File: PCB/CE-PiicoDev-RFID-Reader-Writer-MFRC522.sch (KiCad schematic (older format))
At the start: 63 parts, among them J1 , J2 , J3 Conn_PiicoDev_header_01x04_Ma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, J4 Conn_01x01_Male, J5 Conn_01x01_Male, Q1 BSS138, U1 MFRC522, Y1 27.12MHz 12pF

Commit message: Improve Artwork
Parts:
- added G6: Label_PCB_Art, PiicoDev RFID MFRC522:Art_1, symbol CoreElectronics_Artwork:Label_PCB_Art
- added G7: Label_PCB_Art, PiicoDev RFID MFRC522:Art_2, symbol CoreElectronics_Artwork:Label_PCB_Art
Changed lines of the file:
@@
 Wire Wire Line
 	5400 3500 5400 3400
+$Comp
+L CoreElectronics_Artwork:Label_PCB_Art G7
+U 1 1 61AF4072
+P 4150 6650
+F 0 "G7" H 4278 6696 50  0000 L CNN
+F 1 "Label_PCB_Art" H 4278 6605 50  0000 L CNN
+F 2 "PiicoDev RFID MFRC522:Art_2" H 4150 6650 50  0001 C CNN
+F 3 "" H 4150 6650 50  0001 C CNN
+	1    4150 6650
+	1    0    0    -1
+$EndComp
+$Comp
+L CoreElectronics_Artwork:Label_PCB_Art G6
+U 1 1 61AF4D20
+P 4150 6400
+F 0 "G6" H 4278 6446 50  0000 L CNN
+F 1 "Label_PCB_Art" H 4278 6355 50  0000 L CNN
+F 2 "PiicoDev RFID MFRC522:Art_1" H 4150 6400 50  0001 C CNN
+F 3 "" H 4150 6400 50  0001 C CNN
+	1    4150 6400
+	1    0    0    -1
+$EndComp
 $EndSCHEMATC

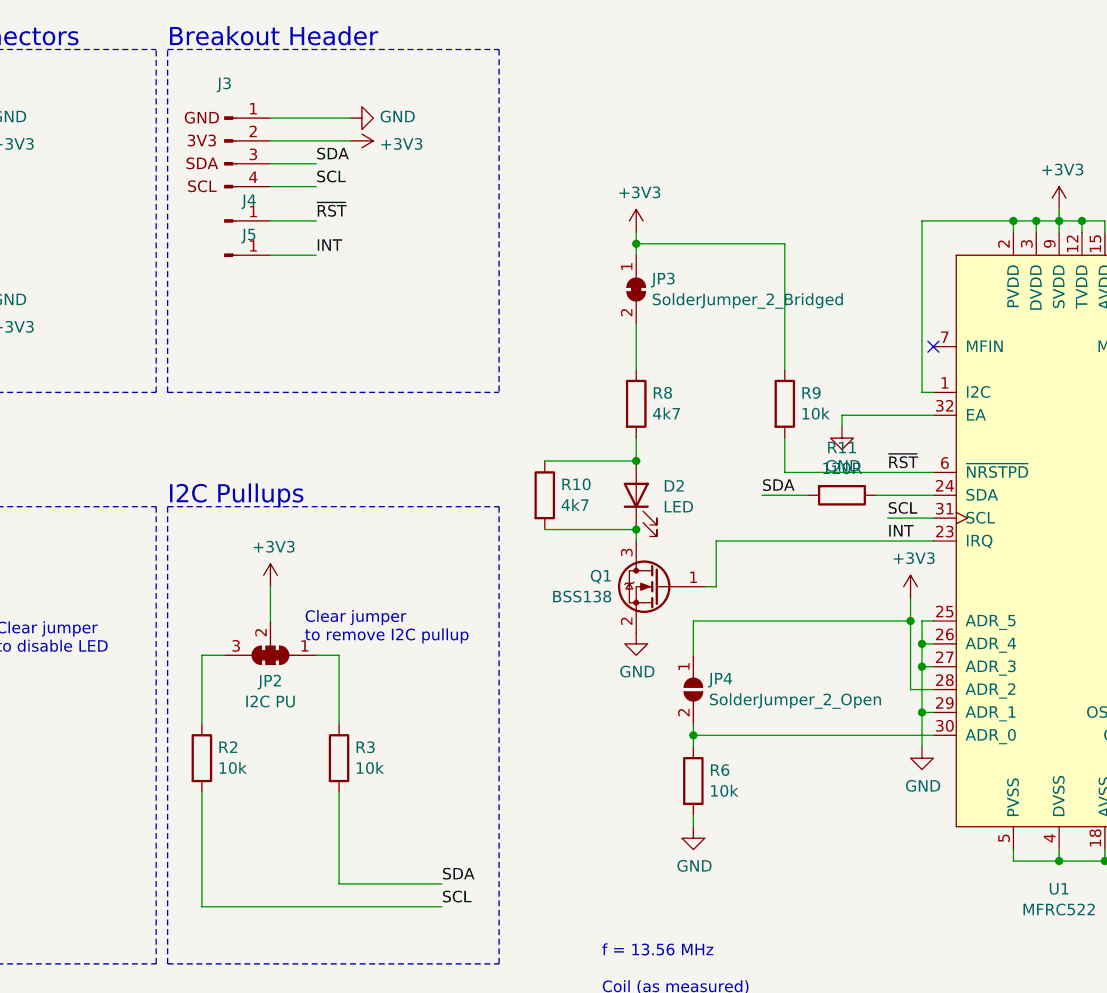
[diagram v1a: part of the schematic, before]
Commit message: Remove Interrupt LED and add DIP switches
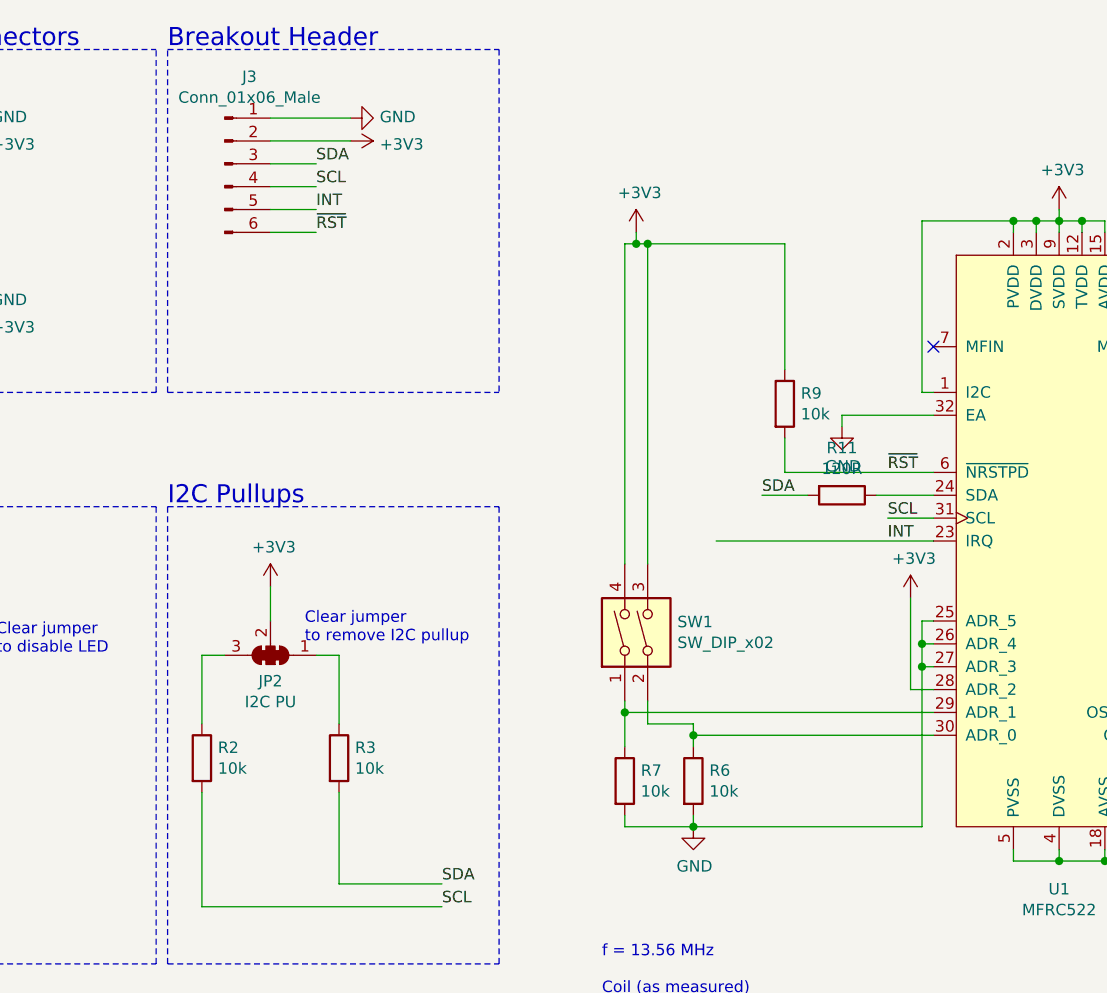
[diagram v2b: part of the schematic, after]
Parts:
- removed D2: LED, CoreElectronics_Components:LED_1206_3216Metric_ReverseMount_Hole1.8x2.4mm, symbol Device:LED
- removed J3: Conn_PiicoDev_header_01x04_Male, CoreElectronics_Components:PiicoDev_header_4pin, symbol CoreElectronics_Components:Conn_PiicoDev_header_01x04_Male
- removed J4: Conn_01x01_Male, CoreElectronics_Components:PiicoDev_header_1pin, symbol Connector:Conn_01x01_Male
- removed J5: Conn_01x01_Male, CoreElectronics_Components:PiicoDev_header_1pin_INT_uninverted, symbol Connector:Conn_01x01_Male
- removed JP3: SolderJumper_2_Bridged, CoreElectronics_Components:SolderJumper-2_P1.3mm_Bridged_RoundedPad1.0x1.5mm, symbol Jumper:SolderJumper_2_Bridged
- removed JP4: SolderJumper_2_Open, CoreElectronics_Components:SolderJumper-2_P1.3mm_Open_RoundedPad1.0x1.5mm, symbol Jumper:SolderJumper_2_Open
- removed Q1: BSS138, Package_TO_SOT_SMD:SOT-23, symbol Transistor_FET:BSS138
- removed R10, R8: 4k7, Resistor_SMD:R_0402_1005Metric, symbol Device:R
- added J3: Conn_01x06_Male, CoreElectronics_Components:PiicoDev_header_6pin, symbol Connector:Conn_01x06_Male
- added R7: 10k, Resistor_SMD:R_0402_1005Metric, symbol Device:R
- added SW1: SW_DIP_x02, CoreElectronics_Components:SW_DIP_x02_Slide_CHS-02A1, symbol Switch:SW_DIP_x02
- G2: footprint CoreElectronics_Artwork:CoreElectronics_logo_5mm -> (none)
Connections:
- net +3V3: now also J3.2 (Pin_2), SW1.3, SW1.4
- net GND: now also J3.1 (Pin_1), R7.2; no longer U1.29 (ADR_1)
- net INT: now also J3.5 (Pin_5)
- net SCL: now also J3.4 (Pin_4)
- net SDA: now also J3.3 (Pin_3)
- net ~RST: now also J3.6 (Pin_6)
- net at R6.1, U1.30 (ADR_0): now also SW1.2
- new net: R7.1, SW1.1, U1.29 (ADR_1)
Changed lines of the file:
@@
 Sheet 1 1
 Title "PiicoDev RFID Reader/Writer MFRC522"
-Date "2021-11-26"
-Rev "02"
+Date "2021-12-14"
+Rev "03"
 Comp "Core Electronics"
 Comment1 "Designed at Core Electronics by Peter Johnston"
@@
 F 0 "G2" H 9900 6044 60  0001 C CNN
 F 1 "LOGO_CoreElectronics_no-text" H 9900 6456 60  0001 C CNN
-F 2 "CoreElectronics_Artwork:CoreElectronics_logo_5mm" H 9900 6250 50  0001 C CNN
+F 2 "" H 9900 6250 50  0001 C CNN
 F 3 "" H 9900 6250 50  0001 C CNN
 	1    9900 6250
@@
 Text Label 2800 1600 0    50   ~ 0
 SCL
-Wire Wire Line
-	2800 1600 2600 1600
 Text Label 2800 1500 0    50   ~ 0
 SDA
-Wire Wire Line
-	2800 1500 2600 1500
 $Comp
 L power:+3V3 #PWR?
@@
 	0    -1   -1   0
 $EndComp
-Wire Wire Line
-	2950 1300 2600 1300
-Wire Wire Line
-	2600 1400 2950 1400
 Text Notes 650  1000 0    79   ~ 0
 PiicoDev Connectors
 Text Notes 2150 1000 0    79   ~ 0
 Breakout Header
-$Comp
-L CoreElectronics_Components:Conn_PiicoDev_header_01x04_Male J?
-U 1 1 609F9B2E
-P 2400 1500
-AR Path="/609C5735/609F9B2E" Ref="J?"  Part="1"
-AR Path="/609F9B2E" Ref="J3"  Part="1"
-F 0 "J3" H 2400 1850 50  0000 C CNN
-F 1 "Conn_PiicoDev_header_01x04_Male" H 2421 1807 50  0001 C CNN
-F 2 "CoreElectronics_Components:PiicoDev_header_4pin" H 2400 1500 50  0001 C CNN
-F 3 "~" H 2400 1500 50  0001 C CNN
-	1    2400 1500
-	1    0    0    -1
-$EndComp
 Wire Notes Line
 	650  2500 650  1000
@@
 	1    0    0    -1
 $EndComp
-$Comp
-L Connector:Conn_01x01_Male J4
-U 1 1 6159070E
-P 2400 1750
-F 0 "J4" H 2508 1839 50  0000 C CNN
-F 1 "Conn_01x01_Male" H 2508 1840 50  0001 C CNN
-F 2 "CoreElectronics_Components:PiicoDev_header_1pin" H 2400 1750 50  0001 C CNN
-F 3 "~" H 2400 1750 50  0001 C CNN
-	1    2400 1750
-	1    0    0    -1
-$EndComp
-$Comp
-L Connector:Conn_01x01_Male J5
-U 1 1 61591567
-P 2400 1900
-F 0 "J5" H 2508 1989 50  0000 C CNN
-F 1 "Conn_01x01_Male" H 2508 1990 50  0001 C CNN
-F 2 "CoreElectronics_Components:PiicoDev_header_1pin_INT_uninverted" H 2400 1900 50  0001 C CNN
-F 3 "~" H 2400 1900 50  0001 C CNN
-	1    2400 1900
-	1    0    0    -1
-$EndComp
-Wire Wire Line
-	2600 1750 2800 1750
-Wire Wire Line
-	2600 1900 2800 1900
-Text Label 2800 1750 0    50   ~ 0
+Text Label 2800 1800 0    50   ~ 0
 ~RST
-Text Label 2800 1900 0    50   ~ 0
+Text Label 2800 1700 0    50   ~ 0
 INT
 Wire Wire Line
 	8150 4550 8150 4600
 Connection ~ 8150 4550
-$Comp
-L Device:LED D2
-U 1 1 6138F2E9
-P 4200 2950
-F 0 "D2" V 4239 2832 50  0000 R CNN
-F 1 "LED" V 4148 2832 50  0000 R CNN
-F 2 "CoreElectronics_Components:LED_1206_3216Metric_ReverseMount_Hole1.8x2.4mm" H 4200 2950 50  0001 C CNN
-F 3 "~" H 4200 2950 50  0001 C CNN
-	1    4200 2950
-	0    -1   -1   0
-$EndComp
-$Comp
-L Device:R R8
-U 1 1 61390113
-P 4200 2550
-F 0 "R8" H 4270 2596 50  0000 L CNN
-F 1 "4k7" H 4270 2505 50  0000 L CNN
-F 2 "Resistor_SMD:R_0402_1005Metric" V 4130 2550 50  0001 C CNN
-F 3 "~" H 4200 2550 50  0001 C CNN
-	1    4200 2550
-	1    0    0    -1
-$EndComp
 $Comp
 L power:+3V3 #PWR0113
@@
 $EndComp
 Wire Wire Line
-	4200 2700 4200 2800
-$Comp
-L Jumper:SolderJumper_2_Bridged JP3
-U 1 1 613A247F
-P 4200 2050
-F 0 "JP3" V 4154 2118 50  0000 L CNN
-F 1 "SolderJumper_2_Bridged" V 4245 2118 50  0000 L CNN
-F 2 "CoreElectronics_Components:SolderJumper-2_P1.3mm_Bridged_RoundedPad1.0x1.5mm" H 4200 2050 50  0001 C CNN
-F 3 "~" H 4200 2050 50  0001 C CNN
-	1    4200 2050
-	0    1    1    0
-$EndComp
-Wire Wire Line
 	4200 1800 4200 1850
-Wire Wire Line
-	4200 2200 4200 2400
-Wire Wire Line
-	4200 3150 4200 3100
 $Comp
 L power:GND #PWR0114
@@
 $EndComp
 Wire Wire Line
-	4200 1850 4850 1850
+	4200 1850 4250 1850
 Wire Wire Line
 	4850 1850 4850 2400
-Connection ~ 4200 1850
-Wire Wire Line
-	4200 1850 4200 1900
 Wire Wire Line
 	4850 2700 4850 2850
@@
 Text Label 10400 3150 0    50   ~ 0
 TURN6A
-Wire Wire Line
-	4550 3150 4550 3350
-Wire Wire Line
-	4550 3350 4500 3350
-$Comp
-L power:GND #PWR05
-U 1 1 6175382D
-P 4200 3550
-F 0 "#PWR05" H 4200 3300 50  0001 C CNN
-F 1 "GND" H 4205 3377 50  0000 C CNN
-F 2 "" H 4200 3550 50  0001 C CNN
-F 3 "" H 4200 3550 50  0001 C CNN
-	1    4200 3550
-	1    0    0    -1
-$EndComp
-$Comp
-L Device:R R10
-U 1 1 6175452D
-P 3800 2950
-F 0 "R10" H 3870 2996 50  0000 L CNN
-F 1 "4k7" H 3870 2905 50  0000 L CNN
-F 2 "Resistor_SMD:R_0402_1005Metric" V 3730 2950 50  0001 C CNN
-F 3 "~" H 3800 2950 50  0001 C CNN
-	1    3800 2950
-	1    0    0    -1
-$EndComp
-Wire Wire Line
-	3800 2800 4200 2800
-Connection ~ 4200 2800
-Wire Wire Line
-	3800 3100 4200 3100
-Connection ~ 4200 3100
 $Comp
 L CoreElectronics_Artwork:Label_PCB_Art G4
@@
 /Design Files/MFRC522.m
 Wire Wire Line
-	4550 3150 5500 3150
-Wire Wire Line
 	4850 2850 5500 2850
-$Comp
-L Transistor_FET:BSS138 Q1
-U 1 1 61721C80
-P 4300 3350
-F 0 "Q1" H 4505 3396 50  0000 L CNN
-F 1 "BSS138" H 4505 3305 50  0000 L CNN
-F 2 "Package_TO_SOT_SMD:SOT-23" H 4500 3275 50  0001 L CIN
-F 3 "https://www.onsemi.com/pub/Collateral/BSS138-D.PDF" H 4300 3350 50  0001 L CNN
-	1    4300 3350
-	-1   0    0    -1
-$EndComp
 $Comp
 L Device:Net-Tie_2 NT8
@@
 Wire Wire Line
 	5500 3700 5450 3700
-Connection ~ 5450 3700
-Wire Wire Line
-	5500 3900 5450 3900
-Connection ~ 5450 3900
-$Comp
-L power:GND #PWR0116
-U 1 1 61A25A71
-P 5450 4050
-F 0 "#PWR0116" H 5450 3800 50  0001 C CNN
-F 1 "GND" H 5455 3877 50  0000 C CNN
-F 2 "" H 5450 4050 50  0001 C CNN
-F 3 "" H 5450 4050 50  0001 C CNN
-	1    5450 4050
-	1    0    0    -1
-$EndComp
 Wire Wire Line
 	8100 2750 8700 2750
@@
 	9450 3550 10400 3550
 Wire Wire Line
-	5450 3700 5450 3900
-Wire Wire Line
 	5500 3800 5400 3800
-Wire Wire Line
-	5400 3800 5400 3500
 $Comp
 L power:+3V3 #PWR0117
@@
 $EndComp
 $Comp
-L Jumper:SolderJumper_2_Open JP4
-U 1 1 61A874F4
-P 4450 3800
-F 0 "JP4" V 4404 3868 50  0000 L CNN
-F 1 "SolderJumper_2_Open" V 4495 3868 50  0000 L CNN
-F 2 "CoreElectronics_Components:SolderJumper-2_P1.3mm_Open_RoundedPad1.0x1.5mm" H 4450 3800 50  0001 C CNN
-F 3 "~" H 4450 3800 50  0001 C CNN
-	1    4450 3800
-	0    1    1    0
-$EndComp
-Wire Wire Line
-	5450 3900 5450 4050
-$Comp
 L Device:R R6
 U 1 1 61A91638
@@
 Wire Wire Line
 	4450 4350 4450 4400
-Wire Wire Line
-	4450 4000 4450 3950
 Connection ~ 4450 4000
-Wire Wire Line
-	4450 3650 4450 3500
-Wire Wire Line
-	4450 3500 5400 3500
-Connection ~ 5400 3500
-Wire Wire Line
-	5400 3500 5400 3400
 $Comp
 L CoreElectronics_Artwork:Label_PCB_Art G7
@@
 	1    0    0    -1
 $EndComp
+$Comp
+L Switch:SW_DIP_x02 SW1
+U 1 1 61B8AD1D
+P 4250 3550
+F 0 "SW1" V 4296 3420 50  0000 R CNN
+F 1 "SW_DIP_x02" V 4205 3420 50  0000 R CNN
+F 2 "CoreElectronics_Components:SW_DIP_x02_Slide_CHS-02A1" H 4250 3550 50  0001 C CNN
+F 3 "~" H 4250 3550 50  0001 C CNN
+	1    4250 3550
+	0    -1   -1   0
+$EndComp
+Wire Wire Line
+	4550 3150 5500 3150
+Wire Wire Line
+	5400 3400 5400 3800
+$Comp
+L Device:R R7
+U 1 1 61B9EEBA
+P 4150 4200
+F 0 "R7" H 4220 4246 50  0000 L CNN
+F 1 "10k" H 4220 4155 50  0000 L CNN
+F 2 "Resistor_SMD:R_0402_1005Metric" V 4080 4200 50  0001 C CNN
+F 3 "~" H 4150 4200 50  0001 C CNN
+	1    4150 4200
+	1    0    0    -1
+$EndComp
+Wire Wire Line
+	4150 4350 4150 4400
+Wire Wire Line
+	4150 4400 4450 4400
+Connection ~ 4450 4400
+Wire Wire Line
+	4150 3250 4150 1850
+Wire Wire Line
+	4150 1850 4200 1850
+Connection ~ 4200 1850
+Wire Wire Line
+	4250 3250 4250 1850
+Connection ~ 4250 1850
+Wire Wire Line
+	4250 1850 4850 1850
+Wire Wire Line
+	4150 3850 4150 3900
+Wire Wire Line
+	4150 3900 4150 4050
+Connection ~ 4150 3900
+Wire Wire Line
+	4250 3850 4250 3950
+Wire Wire Line
+	4250 3950 4450 3950
+Wire Wire Line
+	4450 3950 4450 4000
+Wire Wire Line
+	4150 3900 5500 3900
+Wire Wire Line
+	5450 3700 5450 4400
+Wire Wire Line
+	5450 4400 4450 4400
+Connection ~ 5450 3700
+$Comp
+L Connector:Conn_01x06_Male J3
+U 1 1 61B8B794
+P 2400 1500
+F 0 "J3" H 2508 1881 50  0000 C CNN
+F 1 "Conn_01x06_Male" H 2508 1790 50  0000 C CNN
+F 2 "CoreElectronics_Components:PiicoDev_header_6pin" H 2400 1500 50  0001 C CNN
+F 3 "~" H 2400 1500 50  0001 C CNN
+	1    2400 1500
+	1    0    0    -1
+$EndComp
+Wire Wire Line
+	2600 1300 2950 1300
+Wire Wire Line
+	2600 1400 2950 1400
+Wire Wire Line
+	2600 1500 2800 1500
+Wire Wire Line
+	2600 1600 2800 1600
+Wire Wire Line
+	2600 1700 2800 1700
+Wire Wire Line
+	2600 1800 2800 1800
 $EndSCHEMATC
